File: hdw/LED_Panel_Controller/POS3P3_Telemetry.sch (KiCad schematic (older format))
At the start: 7 parts

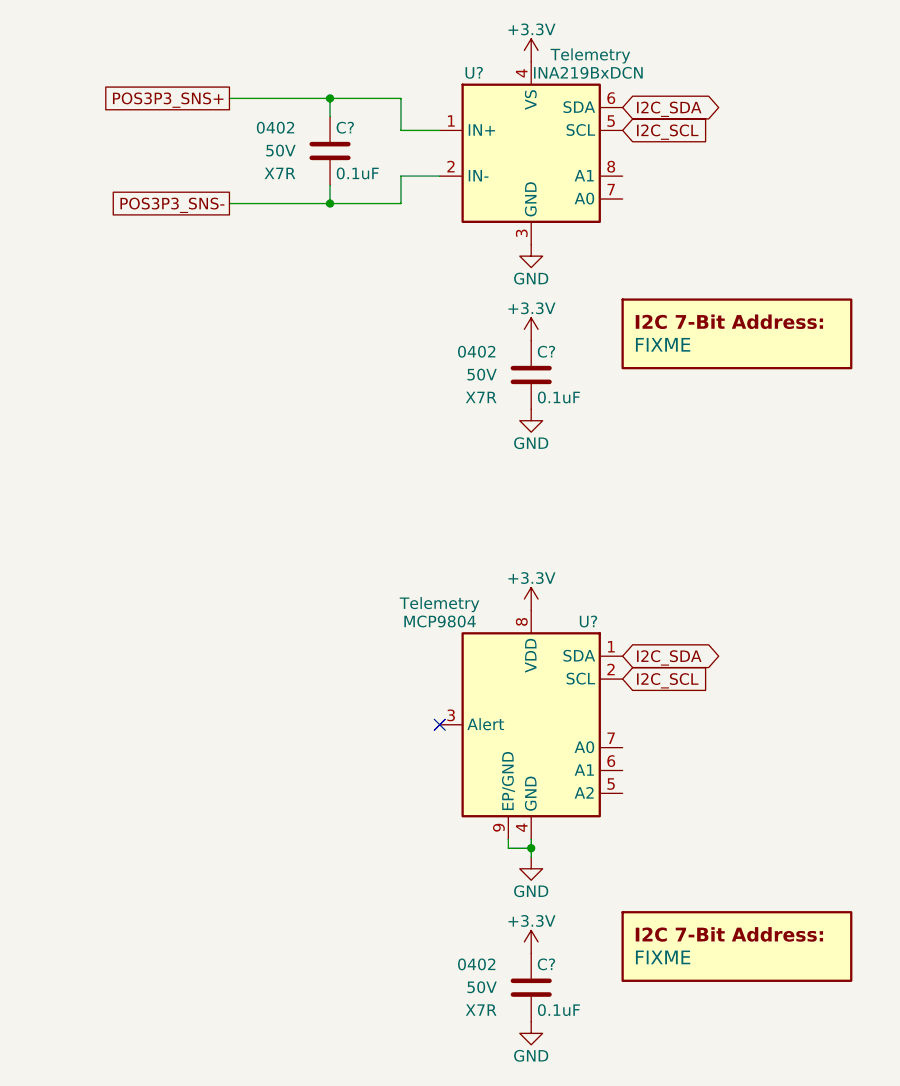
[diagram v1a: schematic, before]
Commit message: fixed level shifter sheet
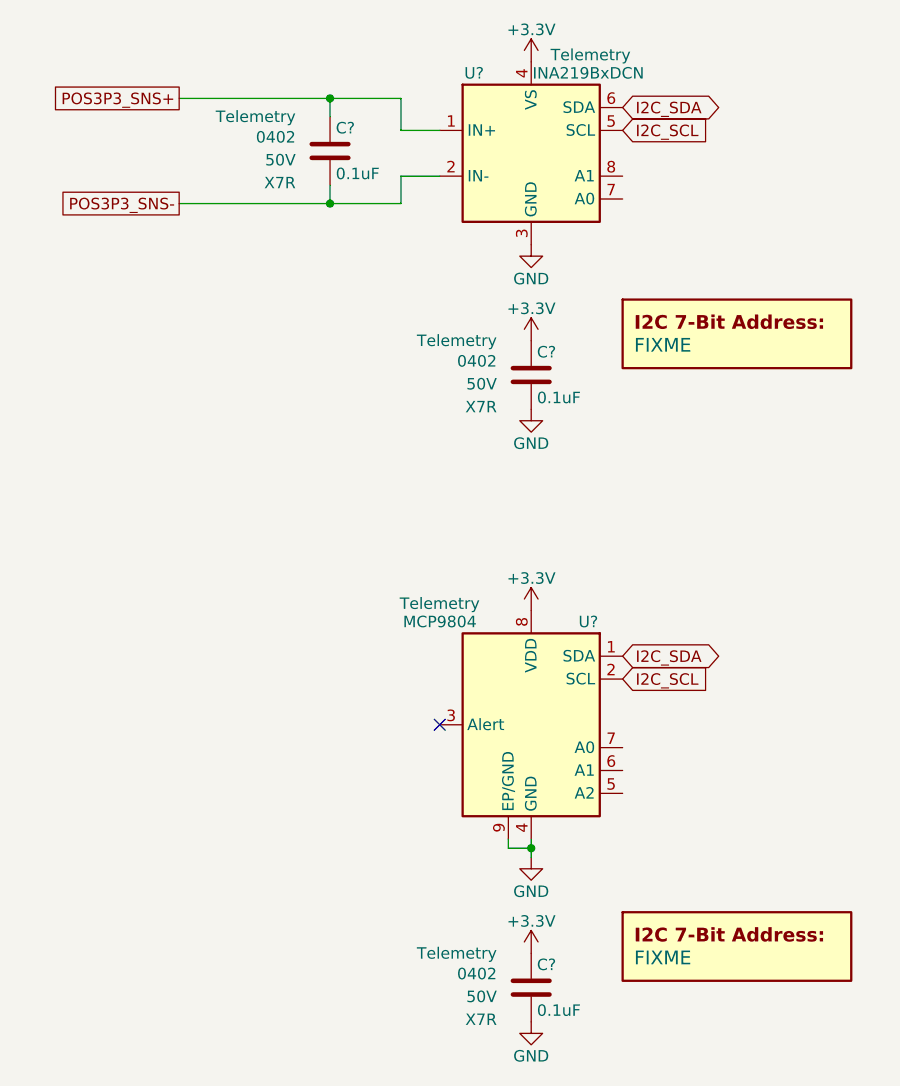
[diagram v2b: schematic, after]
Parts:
- removed C? (x3): 0.1uF, Capacitors_SMD:C_0402, symbol Custom_Library:C_Custom
- added C? (x3): 0.1uF, Capacitors_SMD:C_0402, symbol Custom_Library:C_Custom
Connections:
- net +3V3: now also C?.1, C?.1
- net GND: now also C?.2, C?.2
- net POS3P3_SNS+: now also C?.1
- net POS3P3_SNS-: now also C?.2
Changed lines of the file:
@@
 Comment4 ""
 $EndDescr
-Text GLabel 3790 1800 0    50   UnSpc ~ 0
+Text GLabel 3570 1800 0    50   UnSpc ~ 0
 POS3P3_SNS+
-Text GLabel 3790 2260 0    50   UnSpc ~ 0
+Text GLabel 3570 2260 0    50   UnSpc ~ 0
 POS3P3_SNS-
 $Comp
@@
 Text GLabel 5510 1940 2    50   Input ~ 0
 I2C_SCL
-$Comp
-L Custom_Library:C_Custom C?
-U 1 1 5E0B2427
-P 5110 3010
-AR Path="/5B3E071A/5E0B2427" Ref="C?"  Part="1"
-AR Path="/5E0652BA/5E0B2427" Ref="C?"  Part="1"
-AR Path="/5E0A0E29/5E0B2427" Ref="C?"  Part="1"
-AR Path="/5E052856/5E0B2427" Ref="C?"  Part="1"
-AR Path="/5EAE2D84/5E0B2427" Ref="C?"  Part="1"
-AR Path="/5F581B58/5E0B2427" Ref="C?"  Part="1"
-AR Path="/5F581B77/5E0B2427" Ref="C?"  Part="1"
-F 0 "C?" H 5135 3110 50  0000 L CNN
-F 1 "0.1uF" H 5135 2910 50  0000 L CNN
-F 2 "Capacitors_SMD:C_0402" H 5148 2860 50  0001 C CNN
-F 3 "" H 5135 3110 50  0001 C CNN
-F 4 "0402" H 4960 3110 50  0000 R CNN "display_footprint"
-F 5 "50V" H 4960 3010 50  0000 R CNN "Voltage"
-F 6 "X7R" H 4960 2910 50  0000 R CNN "Dielectric"
-F 7 "" H 1200 -3870 50  0001 C CNN "Digi-Key PN"
-	1    5110 3010
-	1    0    0    -1
-$EndComp
 $Comp
 L power:+3.3V #PWR?
@@
 NoConn ~ 4710 4540
 $Comp
-L Custom_Library:C_Custom C?
-U 1 1 5E2AA9A1
-P 5110 5690
-AR Path="/5B3E071A/5E2AA9A1" Ref="C?"  Part="1"
-AR Path="/5E0652BA/5E2AA9A1" Ref="C?"  Part="1"
-AR Path="/5E0A0E29/5E2AA9A1" Ref="C?"  Part="1"
-AR Path="/5E052856/5E2AA9A1" Ref="C?"  Part="1"
-AR Path="/5EAE2D84/5E2AA9A1" Ref="C?"  Part="1"
-AR Path="/5F581B58/5E2AA9A1" Ref="C?"  Part="1"
-AR Path="/5F581B77/5E2AA9A1" Ref="C?"  Part="1"
-F 0 "C?" H 5135 5790 50  0000 L CNN
-F 1 "0.1uF" H 5135 5590 50  0000 L CNN
-F 2 "Capacitors_SMD:C_0402" H 5148 5540 50  0001 C CNN
-F 3 "" H 5135 5790 50  0001 C CNN
-F 4 "0402" H 4960 5790 50  0000 R CNN "display_footprint"
-F 5 "50V" H 4960 5690 50  0000 R CNN "Voltage"
-F 6 "X7R" H 4960 5590 50  0000 R CNN "Dielectric"
-F 7 "" H 1200 -1190 50  0001 C CNN "Digi-Key PN"
-	1    5110 5690
-	1    0    0    -1
-$EndComp
-$Comp
 L power:+3.3V #PWR?
 U 1 1 5E2AA9A6
@@
 	4230 1880 4230 1800
 $Comp
-L Custom_Library:C_Custom C?
-U 1 1 5E07E0FD
-P 4230 2030
-AR Path="/5B3E071A/5E07E0FD" Ref="C?"  Part="1"
-AR Path="/5E0652BA/5E07E0FD" Ref="C?"  Part="1"
-AR Path="/5E0A0E29/5E07E0FD" Ref="C?"  Part="1"
-AR Path="/5E052856/5E07E0FD" Ref="C?"  Part="1"
-AR Path="/5EAE2D84/5E07E0FD" Ref="C?"  Part="1"
-AR Path="/5F581B58/5E07E0FD" Ref="C?"  Part="1"
-AR Path="/5F581B77/5E07E0FD" Ref="C?"  Part="1"
-F 0 "C?" H 4255 2130 50  0000 L CNN
-F 1 "0.1uF" H 4255 1930 50  0000 L CNN
-F 2 "Capacitors_SMD:C_0402" H 4268 1880 50  0001 C CNN
-F 3 "" H 4255 2130 50  0001 C CNN
-F 4 "0402" H 4080 2130 50  0000 R CNN "display_footprint"
-F 5 "50V" H 4080 2030 50  0000 R CNN "Voltage"
-F 6 "X7R" H 4080 1930 50  0000 R CNN "Dielectric"
-F 7 "" H 320 -4850 50  0001 C CNN "Digi-Key PN"
-	1    4230 2030
-	1    0    0    -1
-$EndComp
-Wire Wire Line
-	3790 2260 4230 2260
-Wire Wire Line
-	3790 1800 4230 1800
-$Comp
 L Analog_ADC:INA219BxDCN U?
 U 1 1 5E1AAC3C
@@
 	4540 2260 4230 2260
 Connection ~ 4230 2260
+$Comp
+L Custom_Library:C_Custom C?
+U 1 1 6018BD18
+P 4230 2030
+AR Path="/5B3E071A/6018BD18" Ref="C?"  Part="1"
+AR Path="/5E0652BA/6018BD18" Ref="C?"  Part="1"
+AR Path="/5E0A0E29/6018BD18" Ref="C?"  Part="1"
+AR Path="/5E052856/6018BD18" Ref="C?"  Part="1"
+AR Path="/5EAE2D84/6018BD18" Ref="C?"  Part="1"
+AR Path="/5F581B58/6018BD18" Ref="C?"  Part="1"
+AR Path="/5F581B77/6018BD18" Ref="C?"  Part="1"
+F 0 "C?" H 4255 2130 50  0000 L CNN
+F 1 "0.1uF" H 4255 1930 50  0000 L CNN
+F 2 "Capacitors_SMD:C_0402" H 4268 1880 50  0001 C CNN
+F 3 "" H 4255 2130 50  0001 C CNN
+F 4 "0402" H 4080 2090 50  0000 R CNN "display_footprint"
+F 5 "50V" H 4080 1990 50  0000 R CNN "Voltage"
+F 6 "X7R" H 4080 1890 50  0000 R CNN "Dielectric"
+F 7 "Telemetry" H 4080 2180 50  0000 R CNN "Configuration"
+	1    4230 2030
+	1    0    0    -1
+$EndComp
+Wire Wire Line
+	3570 1800 4230 1800
+Wire Wire Line
+	3570 2260 4230 2260
+$Comp
+L Custom_Library:C_Custom C?
+U 1 1 6018C640
+P 5110 5690
+AR Path="/5B3E071A/6018C640" Ref="C?"  Part="1"
+AR Path="/5E0652BA/6018C640" Ref="C?"  Part="1"
+AR Path="/5E0A0E29/6018C640" Ref="C?"  Part="1"
+AR Path="/5E052856/6018C640" Ref="C?"  Part="1"
+AR Path="/5EAE2D84/6018C640" Ref="C?"  Part="1"
+AR Path="/5F581B58/6018C640" Ref="C?"  Part="1"
+AR Path="/5F581B77/6018C640" Ref="C?"  Part="1"
+F 0 "C?" H 5135 5790 50  0000 L CNN
+F 1 "0.1uF" H 5135 5590 50  0000 L CNN
+F 2 "Capacitors_SMD:C_0402" H 5148 5540 50  0001 C CNN
+F 3 "" H 5135 5790 50  0001 C CNN
+F 4 "0402" H 4960 5750 50  0000 R CNN "display_footprint"
+F 5 "50V" H 4960 5650 50  0000 R CNN "Voltage"
+F 6 "X7R" H 4960 5550 50  0000 R CNN "Dielectric"
+F 7 "Telemetry" H 4960 5840 50  0000 R CNN "Configuration"
+	1    5110 5690
+	1    0    0    -1
+$EndComp
+$Comp
+L Custom_Library:C_Custom C?
+U 1 1 6018CFFA
+P 5110 3010
+AR Path="/5B3E071A/6018CFFA" Ref="C?"  Part="1"
+AR Path="/5E0652BA/6018CFFA" Ref="C?"  Part="1"
+AR Path="/5E0A0E29/6018CFFA" Ref="C?"  Part="1"
+AR Path="/5E052856/6018CFFA" Ref="C?"  Part="1"
+AR Path="/5EAE2D84/6018CFFA" Ref="C?"  Part="1"
+AR Path="/5F581B58/6018CFFA" Ref="C?"  Part="1"
+AR Path="/5F581B77/6018CFFA" Ref="C?"  Part="1"
+F 0 "C?" H 5135 3110 50  0000 L CNN
+F 1 "0.1uF" H 5135 2910 50  0000 L CNN
+F 2 "Capacitors_SMD:C_0402" H 5148 2860 50  0001 C CNN
+F 3 "" H 5135 3110 50  0001 C CNN
+F 4 "0402" H 4960 3070 50  0000 R CNN "display_footprint"
+F 5 "50V" H 4960 2970 50  0000 R CNN "Voltage"
+F 6 "X7R" H 4960 2870 50  0000 R CNN "Dielectric"
+F 7 "Telemetry" H 4960 3160 50  0000 R CNN "Configuration"
+	1    5110 3010
+	1    0    0    -1
+$EndComp
 $EndSCHEMATC

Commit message: added digikey pns, footprints, bom scrubbed
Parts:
- C? (x3): Digi-Key PN (none) -> 490-10701-1-ND
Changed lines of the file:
@@
 F 6 "X7R" H 4080 1890 50  0000 R CNN "Dielectric"
 F 7 "Telemetry" H 4080 2180 50  0000 R CNN "Configuration"
+F 8 "490-10701-1-ND" H 4230 2030 50  0001 C CNN "Digi-Key PN"
 	1    4230 2030
 	1    0    0    -1
@@
 F 6 "X7R" H 4960 5550 50  0000 R CNN "Dielectric"
 F 7 "Telemetry" H 4960 5840 50  0000 R CNN "Configuration"
+F 8 "490-10701-1-ND" H 5110 5690 50  0001 C CNN "Digi-Key PN"
 	1    5110 5690
 	1    0    0    -1
@@
 F 6 "X7R" H 4960 2870 50  0000 R CNN "Dielectric"
 F 7 "Telemetry" H 4960 3160 50  0000 R CNN "Configuration"
+F 8 "490-10701-1-ND" H 5110 3010 50  0001 C CNN "Digi-Key PN"
 	1    5110 3010
 	1    0    0    -1

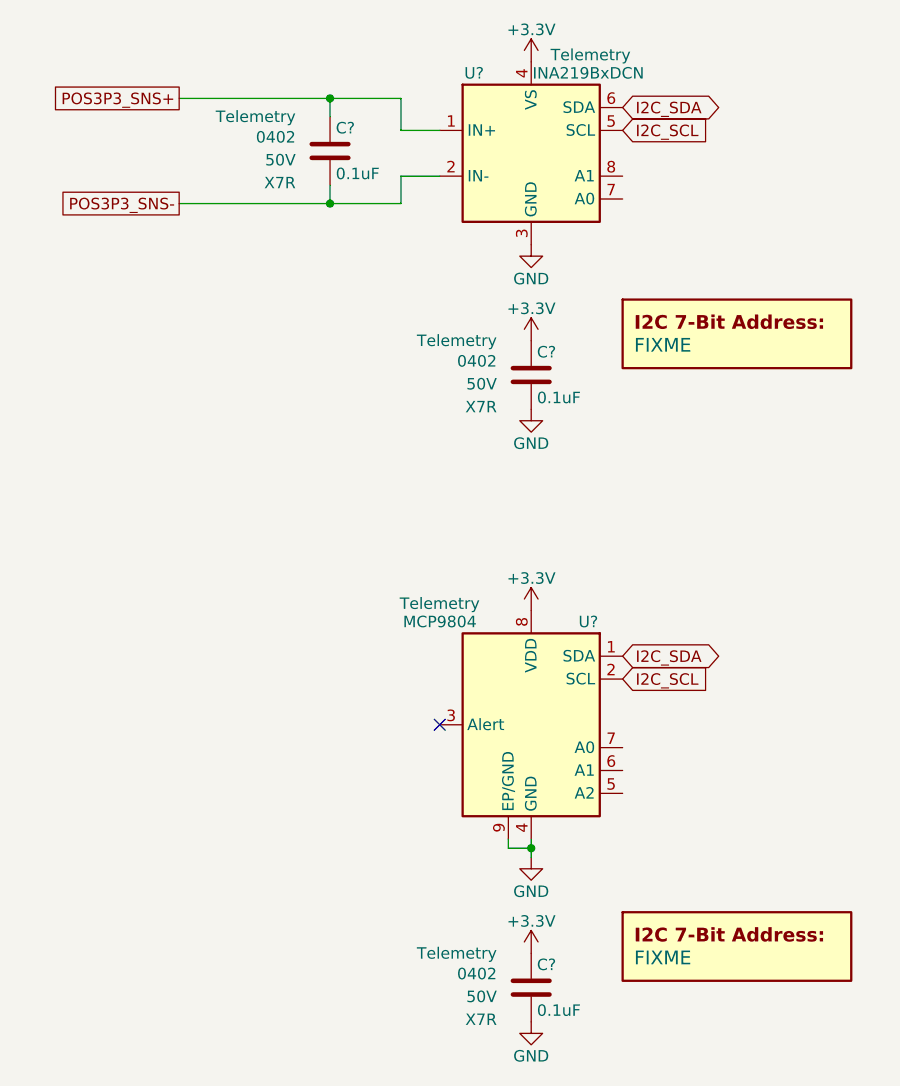
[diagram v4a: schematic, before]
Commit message: assigned I2C addresses
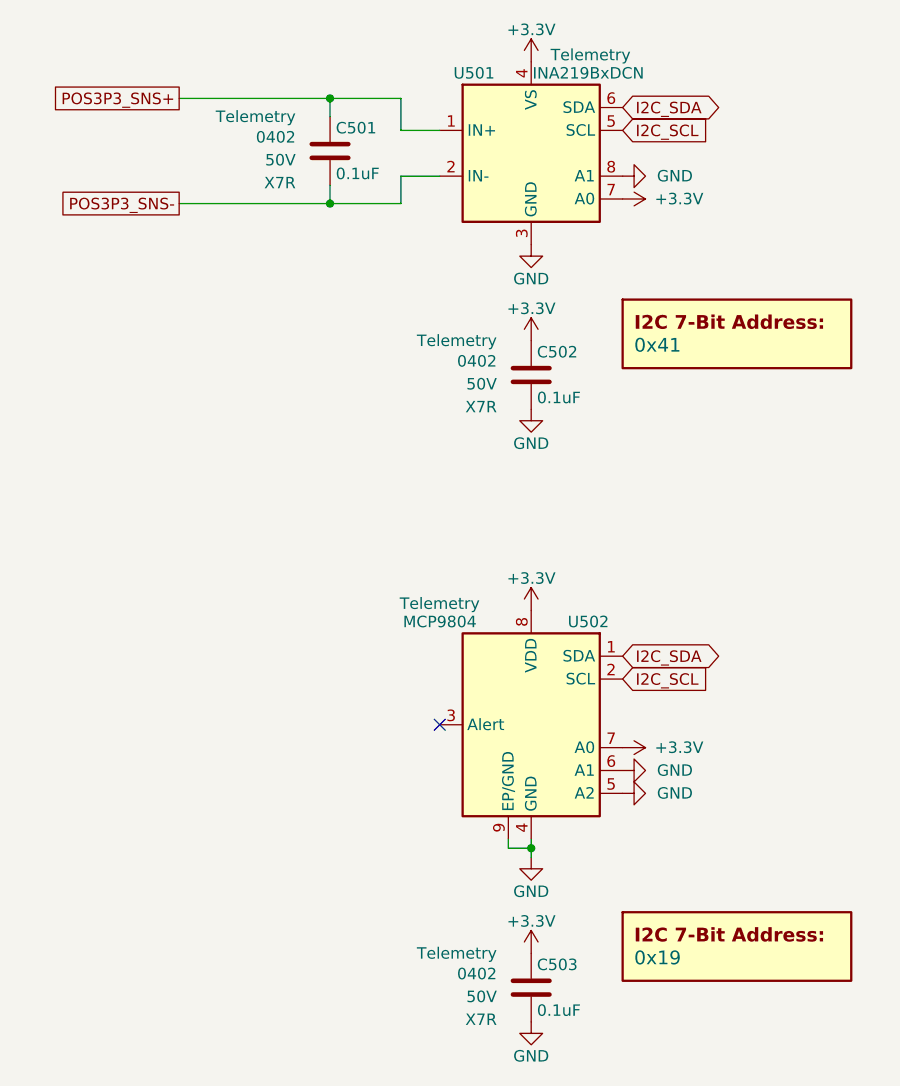
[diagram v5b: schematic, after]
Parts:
- removed DOC?: FIXME, symbol Custom_Library:I2C_Address
- removed U?: INA219BxDCN, Package_TO_SOT_SMD:SOT-23-8, symbol Analog_ADC:INA219BxDCN
- removed U?: MCP9804, Package_DFN_QFN:DFN-8-1EP_3x2mm_P0.5mm_EP1.3x1.5mm, symbol Sensor_Temperature:MCP9804_DFN
- added DOC502: 0x19, symbol Custom_Library:I2C_Address
- added U501: INA219BxDCN, Package_TO_SOT_SMD:SOT-23-8, symbol Analog_ADC:INA219BxDCN
- added U502: MCP9804, Package_DFN_QFN:DFN-8-1EP_3x2mm_P0.5mm_EP1.3x1.5mm, symbol Sensor_Temperature:MCP9804_DFN
- DOC501: renamed from DOC?; value FIXME -> 0x41
- gave numbers to parts that had none: 3
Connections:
- net +3V3: now also U501.4 (VS), U501.7 (A0), U502.7 (A0), U502.8 (VDD)
- net GND: now also U501.3 (GND), U501.8 (A1), U502.4 (GND), U502.5 (A2), U502.6 (A1), U502.9 (EP/GND)
- net I2C_SCL: now also U501.5 (SCL), U502.2 (SCL)
- net I2C_SDA: now also U501.6 (SDA), U502.1 (SDA)
- net POS3P3_SNS+: now also U501.1 (IN+)
- net POS3P3_SNS-: now also U501.2 (IN-)

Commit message: added BOMs, some consolidation
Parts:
- C501, C502, C503: Digi-Key PN 490-10701-1-ND -> 490-10698-1-ND
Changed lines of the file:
@@
 F 6 "X7R" H 4080 1890 50  0000 R CNN "Dielectric"
 F 7 "Telemetry" H 4080 2180 50  0000 R CNN "Configuration"
-F 8 "490-10701-1-ND" H 4230 2030 50  0001 C CNN "Digi-Key PN"
+F 8 "490-10698-1-ND" H 4230 2030 50  0001 C CNN "Digi-Key PN"
 	1    4230 2030
 	1    0    0    -1
@@
 F 6 "X7R" H 4960 5550 50  0000 R CNN "Dielectric"
 F 7 "Telemetry" H 4960 5840 50  0000 R CNN "Configuration"
-F 8 "490-10701-1-ND" H 5110 5690 50  0001 C CNN "Digi-Key PN"
+F 8 "490-10698-1-ND" H 5110 5690 50  0001 C CNN "Digi-Key PN"
 	1    5110 5690
 	1    0    0    -1
@@
 F 6 "X7R" H 4960 2870 50  0000 R CNN "Dielectric"
 F 7 "Telemetry" H 4960 3160 50  0000 R CNN "Configuration"
-F 8 "490-10701-1-ND" H 5110 3010 50  0001 C CNN "Digi-Key PN"
+F 8 "490-10698-1-ND" H 5110 3010 50  0001 C CNN "Digi-Key PN"
 	1    5110 3010
 	1    0    0    -1
